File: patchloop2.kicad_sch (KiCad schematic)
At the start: 12 parts, among them J1 8P8C, J2 Conn_Coaxial, J3 8P8C

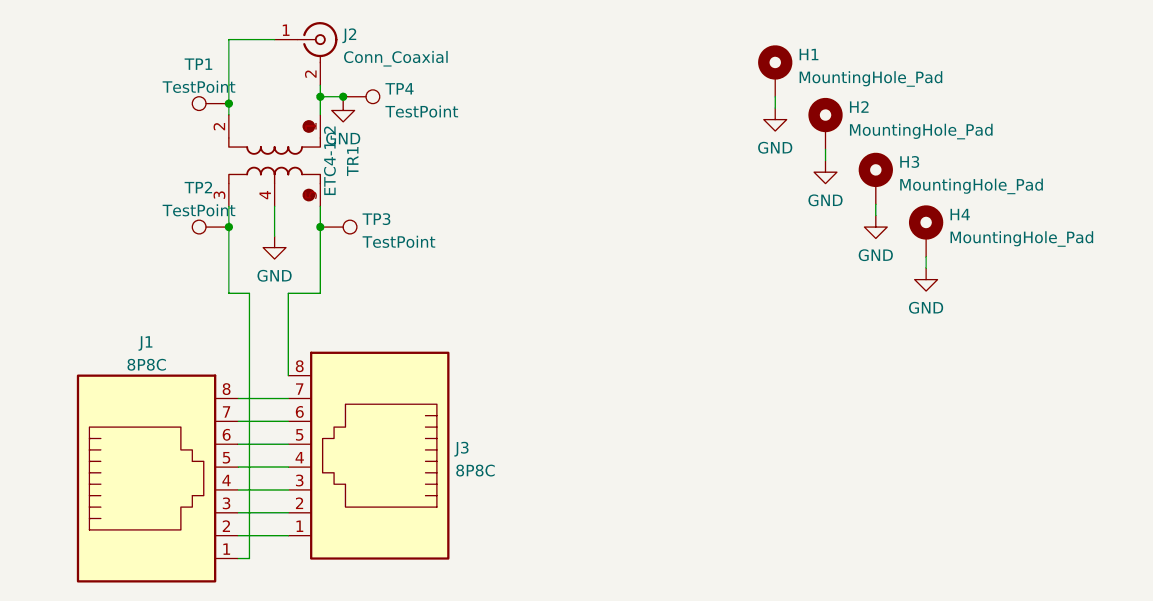
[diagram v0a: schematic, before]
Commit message: Use well known Parts, move to SMD only
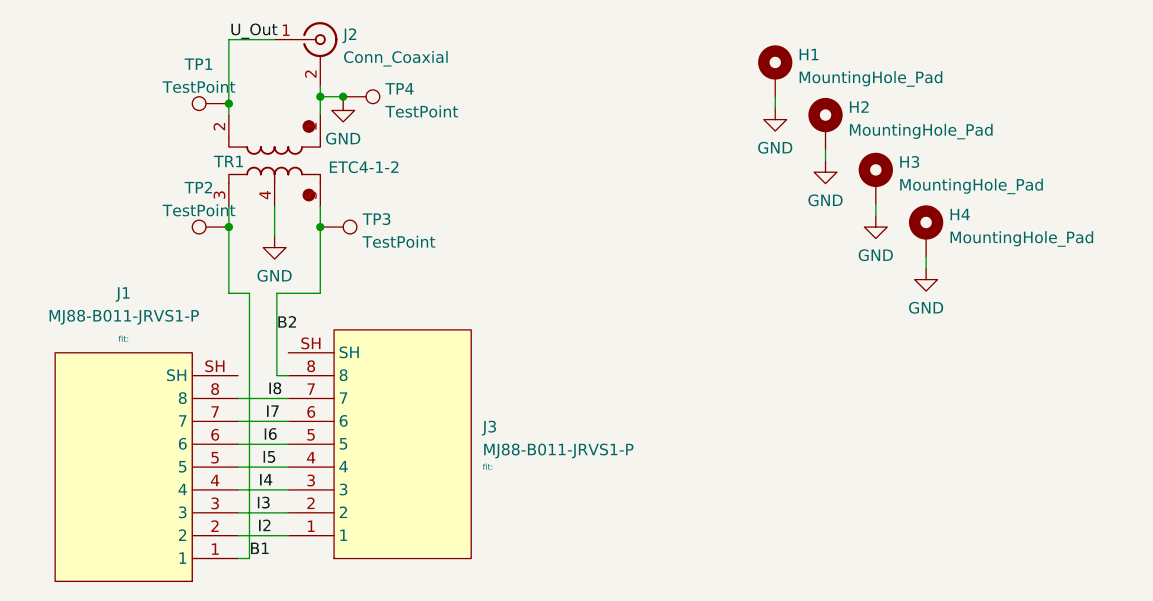
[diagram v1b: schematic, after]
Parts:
- removed J1, J3: 8P8C, Connector_RJ:RJ45_Amphenol_54602-x08_Horizontal, symbol Connector:8P8C
- added J1, J3: MJ88-B011-JRVS1-P, s0_Connector_Heling:MJ88-B011-JRVS1-P, symbol so_Heling:MJ88-B011-JRVS1-P
- J2: footprint Connector_Coaxial:SMA_Samtec_SMA-J-P-X-ST-EM1_EdgeMount -> Connector_Coaxial:SMA_Molex_73251-2200_Horizontal
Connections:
- net U_Out: now reaches J2.1 (In), TP1.1, TR1.2
- net B2: now reaches TP3.1, TR1.5
- net B2: now also J3.8
- net B1: now reaches TP2.1, TR1.3
- net B1: now also J1.1
- new net I2: J1.2, J3.1
- new net I3: J1.3, J3.2
- new net I4: J1.4, J3.3
- new net I5: J1.5, J3.4
- new net I6: J1.6, J3.5
- new net I7: J1.7, J3.6
- new net I8: J1.8, J3.7
